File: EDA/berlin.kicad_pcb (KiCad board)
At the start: 2 copper layers, 133 parts, among them SW1 MXSwitch, SW10 MXSwitch, SW100 MXSwitch, SW101 MXSwitch, SW102 MXSwitch, SW103 MXSwitch, SW104 MXSwitch, SW105-1 MXSwitch, SW105-2 MXSwitch, SW106 MXSwitch, SW107 MXSwitch, SW108 MXSwitch, SW109 MXSwitch, SW11 MXSwitch, SW110 MXSwitch, SW111 MXSwitch, SW112 MXSwitch, SW113 MXSwitch, SW114 MXSwitch, SW115 MXSwitch, SW116 MXSwitch, SW117 MXSwitch, SW118 MXSwitch, SW119 MXSwitch, SW12 MXSwitch, SW120 MXSwitch, SW121 MXSwitch, SW122 MXSwitch, SW123 MXSwitch, SW124-1 MXSwitch, SW124-2 MXSwitch, SW125 MXSwitch, SW126 Rotary_Encoder_Switch_Chassis, SW129 MXSwitch, SW13 MXSwitch, SW14 MXSwitch, SW15 MXSwitch, SW16 MXSwitch, SW17 MXSwitch, SW18 MXSwitch, SW19 MXSwitch, SW2 MXSwitch, SW20-1 MXSwitch, SW21 MXSwitch, SW22 MXSwitch, SW23 MXSwitch, SW24 MXSwitch, SW25 MXSwitch, SW26 MXSwitch, SW27 MXSwitch, SW28 MXSwitch, SW29 MXSwitch, SW3 MXSwitch, SW30 MXSwitch, SW31 MXSwitch, SW32 MXSwitch, SW33 MXSwitch, SW34 MXSwitch, SW35 MXSwitch, SW36 MXSwitch, SW37 MXSwitch, SW38 MXSwitch, SW39-1 MXSwitch, SW39-3 MXSwitch, SW4-2 MXSwitch, SW40 MXSwitch, SW41 MXSwitch, SW42 MXSwitch, SW43 MXSwitch, SW44 MXSwitch, SW45 MXSwitch, SW46 MXSwitch, SW47 MXSwitch, SW48 MXSwitch, SW49 MXSwitch, SW5-1 MXSwitch, SW50 MXSwitch, SW51 MXSwitch, SW52 MXSwitch, SW53 MXSwitch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

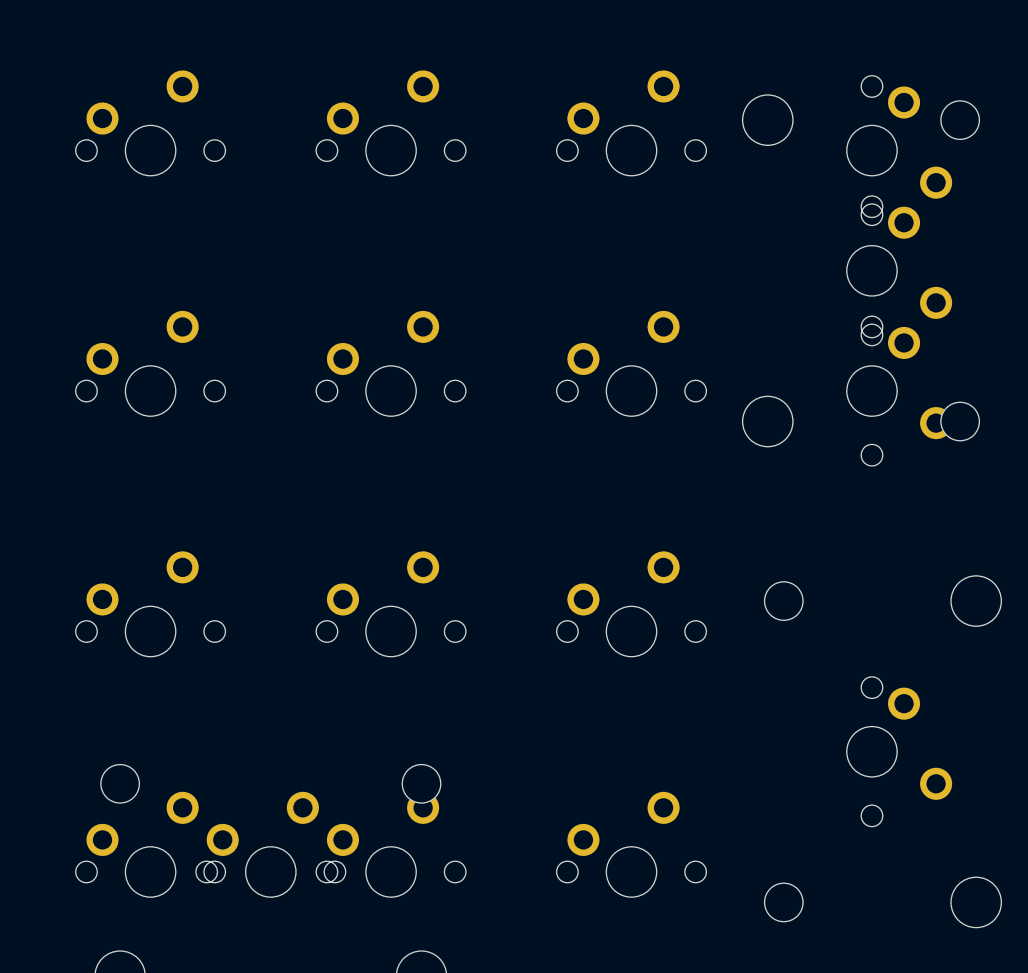
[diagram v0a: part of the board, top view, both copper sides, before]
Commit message: update gitignore and remove unnecessary switches
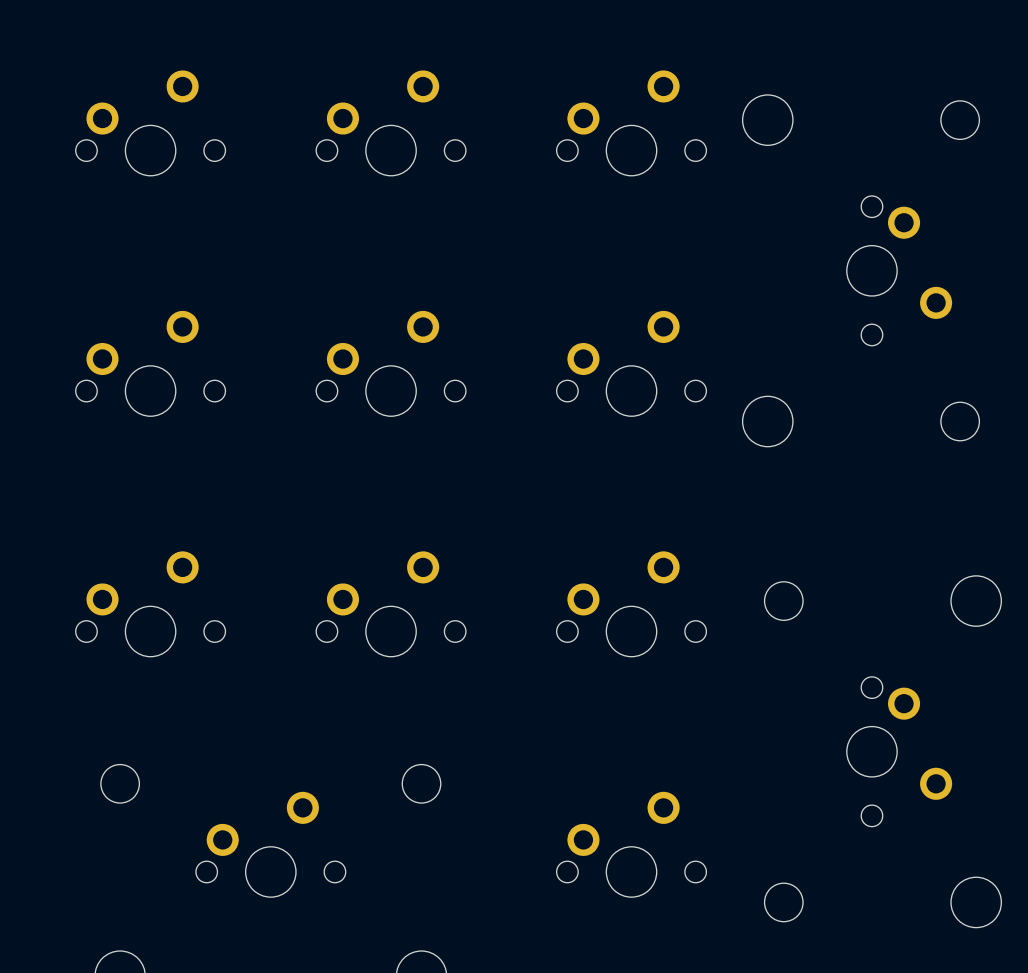
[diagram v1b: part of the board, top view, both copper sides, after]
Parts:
- removed SW105-2, SW112: MXSwitch, acheron_MX:MX100
- removed SW123, SW124-2: MXSwitch, Acheron_MX:MX100

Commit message: bruder muss los
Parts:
- removed the REF** at (441.3, 60.5)
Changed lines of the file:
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@@
     (40 "Dwgs.User" user "User.Drawings")
     (41 "Cmts.User" user "User.Comments")
-    (42 "Eco1.User" user "User.Eco1")
-    (43 "Eco2.User" user "User.Eco2")
     (44 "Edge.Cuts" user)
     (45 "Margin" user)
@@
   )
   (setup
+    (stackup
+      (layer "F.SilkS" (type "Top Silk Screen"))
+      (layer "F.Paste" (type "Top Solder Paste"))
+      (layer "F.Mask" (type "Top Solder Mask") (color "Green") (thickness 0.01))
+      (layer "F.Cu" (type "copper") (thickness 0.035))
+      (layer "dielectric 1" (type "core") (thickness 1.51) (material "FR4") (epsilon_r 4.5) (loss_tangent 0.02))
+      (layer "B.Cu" (type "copper") (thickness 0.035))
+      (layer "B.Mask" (type "Bottom Solder Mask") (color "Green") (thickness 0.01))
+      (layer "B.Paste" (type "Bottom Solder Paste"))
+      (layer "B.SilkS" (type "Bottom Silk Screen"))
+      (copper_finish "None")
+      (dielectric_constraints no)
+    )
     (pad_to_mask_clearance 0)
     (pcbplotparams
@@
     (property "Sheetname" "")
     (attr through_hole)
-    (fp_text reference "SW126" (at 0 0 90) (layer "F.SilkS")
-      (effects (font (size 1 1) (thickness 0.15)))
-    )
-    (fp_text value "Rotary_Encoder_Switch_Chassis" (at 0 -2.5 90) (layer "F.Fab")
+    (fp_text reference "SW126" (at 8.636 -0.12) (layer "F.SilkS")
+      (effects (font (size 1 1) (thickness 0.15)))
+    )
+    (fp_text value "Rotary_Encoder_Switch_Chassis" (at 10.16 0.134) (layer "F.Fab")
       (effects (font (size 1 1) (thickness 0.15)))
     )
@@
     )
   )
-  (footprint "Display:EA_DOGXL160-7_Backlight" (layer "F.Cu")
-    (at 441.325 60.475 -90)
-    (descr "Grapchical,Display,LCD,160x104 http://www.lcd-module.com/eng/pdf/grafik/dogxl160-7e.pdf")
-    (tags "EA_DOGXL160-7_Backlight")
-    (attr through_hole)
-    (fp_text reference "REF**" (at 0.18 -21.02 90) (layer "F.SilkS")
-      (effects (font (size 1 1) (thickness 0.15)))
-    )
-    (fp_text value "EA_DOGXL160-7_Backlight" (at 7.91 59.51 90) (layer "F.Fab")
-      (effects (font (size 1 1) (thickness 0.15)))
-    )
-    (fp_text user "${REFERENCE}" (at 30.48 20.32 90) (layer "F.Fab")
-      (effects (font (size 1 1) (thickness 0.1)))
-    )
-    (fp_line (start -1.82 -20.09) (end -1.82 58.19) (layer "F.SilkS") (width 0.12))
-    (fp_line (start 0.2 -1.35) (end -1.35 -1.35) (layer "F.SilkS") (width 0.12))
-    (fp_line (start -1.82 58.19) (end 62.48 58.19) (layer "F.SilkS") (width 0.12))
-    (fp_line (start 3.1 57.6) (end 55 57.6) (layer "F.SilkS") (width 0.12))
-    (fp_line (start 62.48 -20.09) (end -1.82 -20.09) (layer "F.SilkS") (width 0.12))
-    (fp_line (start -1.35 -1.35) (end -1.35 1) (layer "F.SilkS") (width 0.12))
-    (fp_line (start 62.48 58.19) (end 62.48 -20.09) (layer "F.SilkS") (width 0.12))
-    (fp_line (start 55 57.6) (end 55 -19.5) (layer "F.SilkS") (width 0.12))
-    (fp_line (start 55 -19.5) (end 3.1 -19.5) (layer "F.SilkS") (width 0.12))
-    (fp_line (start 3.1 -19.5) (end 3.1 57.6) (layer "F.SilkS") (width 0.12))
-    (fp_line (start -1.92 -20.2) (end 62.58 -20.2) (layer "F.CrtYd") (width 0.05))
-    (fp_line (start -1.92 58.3) (end -1.92 -20.2) (layer "F.CrtYd") (width 0.05))
-    (fp_line (start 62.58 -20.2) (end 62.58 58.3) (layer "F.CrtYd") (width 0.05))
-    (fp_line (start 62.58 58.3) (end -1.92 58.3) (layer "F.CrtYd") (width 0.05))
-    (fp_line (start 0.34 0) (end -1.66 2) (layer "F.Fab") (width 0.1))
-    (fp_line (start -1.66 -19.95) (end 62.33 -19.95) (layer "F.Fab") (width 0.1))
-    (fp_line (start -1.67 2) (end -1.67 58.05) (layer "F.Fab") (width 0.1))
-    (fp_line (start -1.66 -2) (end -1.66 -19.95) (layer "F.Fab") (width 0.1))
-    (fp_line (start -1.66 -2) (end 0.34 0) (layer "F.Fab") (width 0.1))
-    (fp_line (start 62.33 58.05) (end -1.67 58.05) (layer "F.Fab") (width 0.1))
-    (fp_line (start 62.33 -19.95) (end 62.33 58.05) (layer "F.Fab") (width 0.1))
-    (pad "1" thru_hole rect locked (at 0 0 270) (size 1.524 1.524) (drill 0.762) (layers *.Cu *.Mask))
-    (pad "2" thru_hole circle locked (at 0 2.54 270) (size 1.524 1.524) (drill 0.762) (layers *.Cu *.Mask))
-    (pad "3" thru_hole circle locked (at 0 5.08 270) (size 1.524 1.524) (drill 0.762) (layers *.Cu *.Mask))
-    (pad "14" thru_hole circle locked (at 0 33.02 270) (size 1.524 1.524) (drill 0.762) (layers *.Cu *.Mask))
-    (pad "15" thru_hole circle locked (at 0 35.56 270) (size 1.524 1.524) (drill 0.762) (layers *.Cu *.Mask))
-    (pad "16" thru_hole circle locked (at 0 38.1 270) (size 1.524 1.524) (drill 0.762) (layers *.Cu *.Mask))
-    (pad "17" thru_hole circle locked (at 60.96 38.1 270) (size 1.524 1.524) (drill 0.762) (layers *.Cu *.Mask))
-    (pad "18" thru_hole circle locked (at 60.96 35.56 270) (size 1.524 1.524) (drill 0.762) (layers *.Cu *.Mask))
-    (pad "19" thru_hole circle locked (at 60.96 33.02 270) (size 1.524 1.524) (drill 0.762) (layers *.Cu *.Mask))
-    (pad "20" thru_hole circle locked (at 60.96 30.48 270) (size 1.524 1.524) (drill 0.762) (layers *.Cu *.Mask))
-    (pad "21" thru_hole circle locked (at 60.96 27.94 270) (size 1.524 1.524) (drill 0.762) (layers *.Cu *.Mask))
-    (pad "22" thru_hole circle locked (at 60.96 25.4 270) (size 1.524 1.524) (drill 0.762) (layers *.Cu *.Mask))
-    (pad "23" thru_hole circle locked (at 60.96 22.86 270) (size 1.524 1.524) (drill 0.762) (layers *.Cu *.Mask))
-    (pad "24" thru_hole circle locked (at 60.96 20.32 270) (size 1.524 1.524) (drill 0.762) (layers *.Cu *.Mask))
-    (pad "25" thru_hole circle locked (at 60.96 17.78 270) (size 1.524 1.524) (drill 0.762) (layers *.Cu *.Mask))
-    (pad "26" thru_hole circle locked (at 60.96 15.24 270) (size 1.524 1.524) (drill 0.762) (layers *.Cu *.Mask))
-    (pad "27" thru_hole circle locked (at 60.96 12.7 270) (size 1.524 1.524) (drill 0.762) (layers *.Cu *.Mask))
-    (pad "28" thru_hole circle locked (at 60.96 10.16 270) (size 1.524 1.524) (drill 0.762) (layers *.Cu *.Mask))
-    (pad "29" thru_hole circle locked (at 60.96 7.62 270) (size 1.524 1.524) (drill 0.762) (layers *.Cu *.Mask))
-    (pad "30" thru_hole circle locked (at 60.96 5.08 270) (size 1.524 1.524) (drill 0.762) (layers *.Cu *.Mask))
-    (pad "31" thru_hole circle locked (at 60.96 2.54 270) (size 1.524 1.524) (drill 0.762) (layers *.Cu *.Mask))
-    (pad "32" thru_hole circle locked (at 60.96 0 270) (size 1.524 1.524) (drill 0.762) (layers *.Cu *.Mask))
-    (model "${KICAD6_3DMODEL_DIR}/Display.3dshapes/EA_DOGXL160-7_Backlight.wrl"
-      (offset (xyz 0 0 0))
-      (scale (xyz 1 1 1))
-      (rotate (xyz 0 0 0))
-    )
-  )
   (footprint "acheronHardware:ALPS_EC11E" (layer "F.Cu")
     (at 369.8875 69.85 90)
@@
     (property "Sheetname" "")
     (attr through_hole)
-    (fp_text reference "SW126" (at 0 0 90) (layer "F.SilkS")
-      (effects (font (size 1 1) (thickness 0.15)))
-    )
-    (fp_text value "Rotary_Encoder_Switch_Chassis" (at 0 -2.5 90) (layer "F.Fab")
+    (fp_text reference "SW126" (at 8.89 -0.0635) (layer "F.SilkS")
+      (effects (font (size 1 1) (thickness 0.15)))
+    )
+    (fp_text value "Rotary_Encoder_Switch_Chassis" (at 10.414 -0.0635) (layer "F.Fab")
       (effects (font (size 1 1) (thickness 0.15)))
     )
@@
     (property "Sheetname" "")
     (attr through_hole)
-    (fp_text reference "SW124-1" (at 0 -3.175 90) (layer "Cmts.User")
-      (effects (font (size 1 1) (thickness 0.15) italic))
-    )
-    (fp_text value "MXSwitch" (at 0 -8.7 90) (layer "Cmts.User")
+    (fp_text reference "SW124-1" (at -12.1285 0.03175) (layer "Cmts.User")
+      (effects (font (size 1 1) (thickness 0.15) italic))
+    )
+    (fp_text value "MXSwitch" (at -14.1605 0.03175) (layer "Cmts.User")
       (effects (font (size 1 1) (thickness 0.15)))
     )
@@
     (property "Sheetname" "")
     (attr through_hole)
-    (fp_text reference "SW125" (at 0 -3.175 90) (layer "Cmts.User")
-      (effects (font (size 1 1) (thickness 0.15) italic))
-    )
-    (fp_text value "MXSwitch" (at 0 -6.985 90) (layer "Cmts.User")
-      (effects (font (size 1 1) (thickness 0.15)))
-    )
+    (fp_text reference "SW125" (at -12.1285 0.03175) (layer "Cmts.User")
+      (effects (font (size 1 1) (thickness 0.15) italic))
+    )
+    (fp_text value "MXSwitch" (at -14.1605 0.03175) (layer "Cmts.User")
+      (effects (font (size 1 1) (thickness 0.15)))
+    )

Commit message: update/fix switch descriptors
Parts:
- SW125: value MXSwitch -> 2,19
- renumbered SW126 to SW1,1, SW58 to SW1,10, SW65 to SW1,11, SW72 to SW1,12, SW79 to SW1,13, SW86 to SW1,14, SW93 to SW1,15, SW126 to SW1,16, SW7 to SW1,2, SW14 to SW1,3, SW21 to SW1,4, SW27 to SW1,5, SW33 to SW1,6, SW40 to SW1,7, SW46 to SW1,8, SW52 to SW1,9, SW1 to SW2,1, SW59 to SW2,10, SW66 to SW2,11, SW73 to SW2,12, SW80 to SW2,13, SW86 to SW2,14, SW93 to SW2,15, SW99 to SW2,16, SW122 to SW2,17, SW124-1 to SW2,18, SW8 to SW2,2, SW15 to SW2,3, SW22 to SW2,4, SW28 to SW2,5, SW34 to SW2,6, SW41 to SW2,7, SW47 to SW2,8, SW53 to SW2,9, SW2 to SW3,1, SW60 to SW3,10, SW67 to SW3,11, SW74 to SW3,12, SW81 to SW3,13, SW87 to SW3,14, SW94 to SW3,15, SW100 to SW3,16, SW101 to SW3,17, SW108 to SW3,18, SW115 to SW3,19, SW9 to SW3,2, SW16 to SW3,3, SW23 to SW3,4, SW29 to SW3,5, SW35 to SW3,6, SW42 to SW3,7, SW48 to SW3,8, SW54 to SW3,9, SW3 to SW4,1, SW61 to SW4,10, SW68 to SW4,11, SW75 to SW4,12, SW88-2 to SW4,13, SW106 to SW4,14, SW113 to SW4,15, SW120 to SW4,16, SW102 to SW4,17, SW109 to SW4,18, SW116 to SW4,19, SW10 to SW4,2, SW17 to SW4,3, SW24 to SW4,4, SW30 to SW4,5, SW36 to SW4,6, SW43 to SW4,7, SW49 to SW4,8, SW55 to SW4,9, SW4-2 to SW5,1, SW62 to SW5,10, SW69 to SW5,11, SW76 to SW5,12, SW82 to SW5,13, SW107 to SW5,14, SW114 to SW5,15, SW121 to SW5,16, SW103 to SW5,17, SW110 to SW5,18, SW117 to SW5,19, SW11 to SW5,2, SW18 to SW5,3, SW25 to SW5,4, SW31 to SW5,5, SW37 to SW5,6, SW44 to SW5,7, SW50 to SW5,8, SW56 to SW5,9, SW5-1 to SW6,1, SW63 to SW6,10, SW70 to SW6,11, SW83 to SW6,12, SW90-2 to SW6,13, SW91 to SW6,15, SW104 to SW6,17, SW111 to SW6,18, SW118 to SW6,19, SW12 to SW6,2, SW19 to SW6,3, SW26 to SW6,4, SW32 to SW6,5, SW38 to SW6,6, SW45 to SW6,7, SW51 to SW6,8, SW57 to SW6,9, SW6-1 to SW7,1, SW20-1 to SW7,10, SW20-1 to SW7,11, SW77 to SW7,12, SW129 to SW7,13, SW85 to SW7,14, SW92 to SW7,15, SW98 to SW7,16, SW105-1 to SW7,17, SW119 to SW7,19, SW13 to SW7,2, SW39-3 to SW7,3, SW39-1 to SW7,6, SW20-1 to SW7,8, SW20-1 to SW7,9

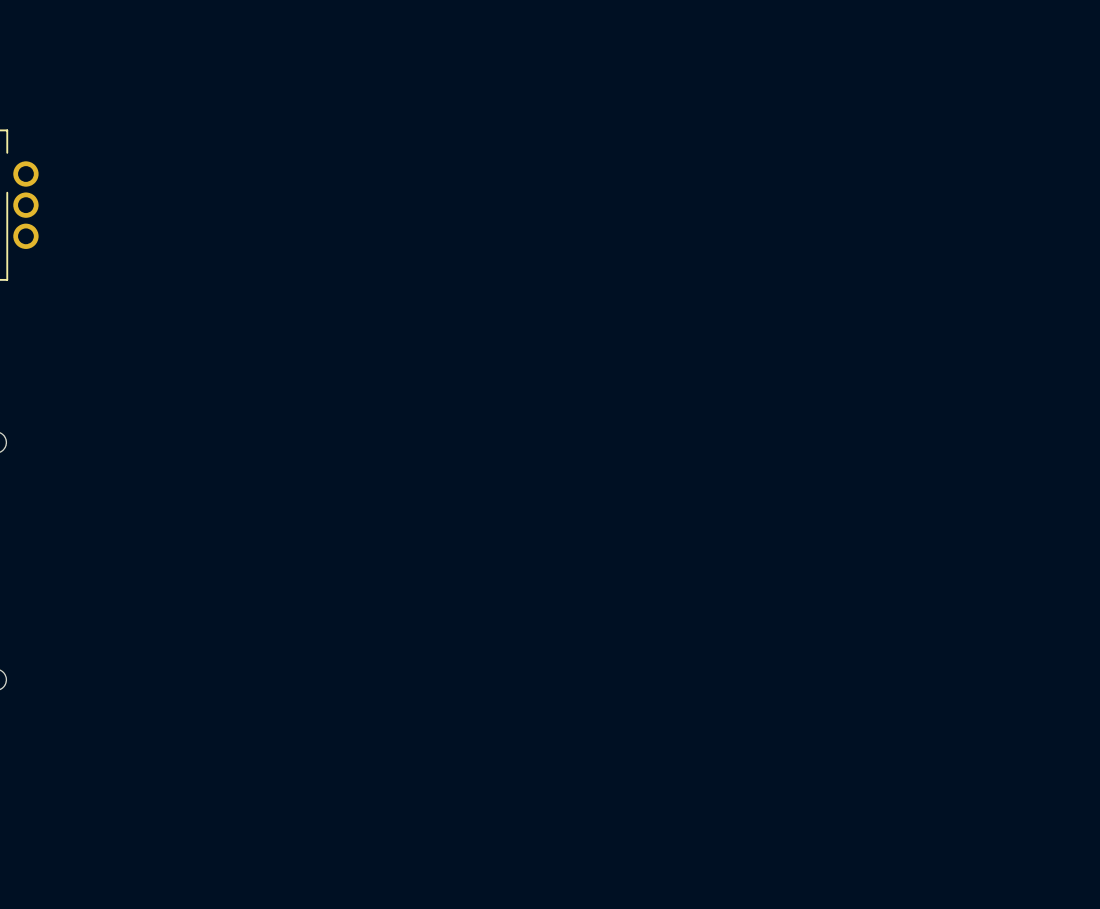
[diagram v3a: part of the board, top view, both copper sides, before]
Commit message: Add DOGXL LCD to PCB
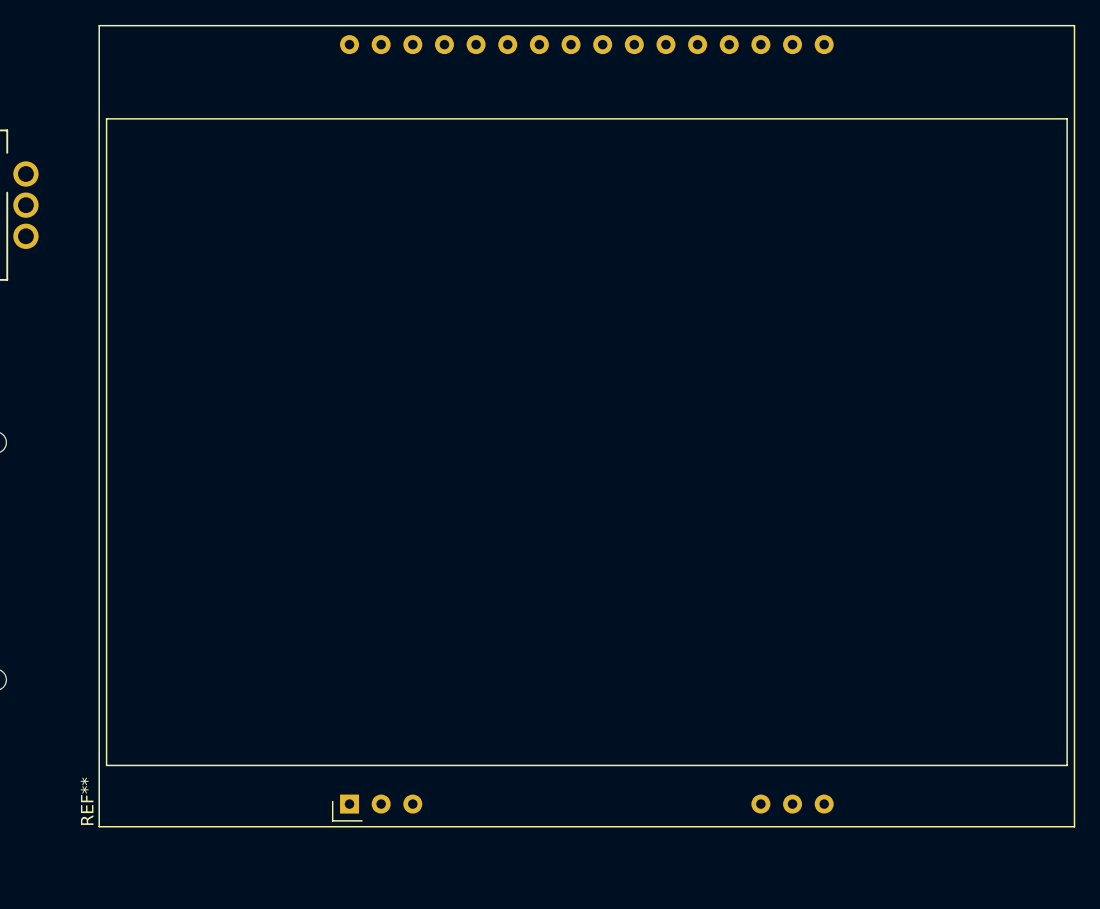
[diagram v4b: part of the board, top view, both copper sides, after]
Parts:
- added REF**: EA_DOGXL160-7_Backlight, Display:EA_DOGXL160-7_Backlight, F.Cu at (403.4, 117.9)
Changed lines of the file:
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@@
+    )
+  )
+  (footprint "Display:EA_DOGXL160-7_Backlight" (layer "F.Cu")
+    (at 403.359915 117.923454 90)
+    (descr "Grapchical,Display,LCD,160x104 http://www.lcd-module.com/eng/pdf/grafik/dogxl160-7e.pdf")
+    (tags "EA_DOGXL160-7_Backlight")
+    (attr through_hole)
+    (fp_text reference "REF**" (at 0.18 -21.02 90) (layer "F.SilkS")
+      (effects (font (size 1 1) (thickness 0.15)))
+    )
+    (fp_text value "EA_DOGXL160-7_Backlight" (at 7.91 59.51 90) (layer "F.Fab")
+      (effects (font (size 1 1) (thickness 0.15)))
+    )
+    (fp_text user "${REFERENCE}" (at 30.48 20.32 90) (layer "F.Fab")
+      (effects (font (size 1 1) (thickness 0.1)))
+    )
+    (fp_line (start -1.82 58.19) (end 62.48 58.19) (layer "F.SilkS") (width 0.12))
+    (fp_line (start 62.48 58.19) (end 62.48 -20.09) (layer "F.SilkS") (width 0.12))
+    (fp_line (start 55 -19.5) (end 3.1 -19.5) (layer "F.SilkS") (width 0.12))
+    (fp_line (start 0.2 -1.35) (end -1.35 -1.35) (layer "F.SilkS") (width 0.12))
+    (fp_line (start -1.35 -1.35) (end -1.35 1) (layer "F.SilkS") (width 0.12))
+    (fp_line (start 62.48 -20.09) (end -1.82 -20.09) (layer "F.SilkS") (width 0.12))
+    (fp_line (start 55 57.6) (end 55 -19.5) (layer "F.SilkS") (width 0.12))
+    (fp_line (start -1.82 -20.09) (end -1.82 58.19) (layer "F.SilkS") (width 0.12))
+    (fp_line (start 3.1 -19.5) (end 3.1 57.6) (layer "F.SilkS") (width 0.12))
+    (fp_line (start 3.1 57.6) (end 55 57.6) (layer "F.SilkS") (width 0.12))
+    (fp_line (start 62.58 58.3) (end -1.92 58.3) (layer "F.CrtYd") (width 0.05))
+    (fp_line (start -1.92 58.3) (end -1.92 -20.2) (layer "F.CrtYd") (width 0.05))
+    (fp_line (start 62.58 -20.2) (end 62.58 58.3) (layer "F.CrtYd") (width 0.05))
+    (fp_line (start -1.92 -20.2) (end 62.58 -20.2) (layer "F.CrtYd") (width 0.05))
+    (fp_line (start -1.66 -19.95) (end 62.33 -19.95) (layer "F.Fab") (width 0.1))
+    (fp_line (start 62.33 -19.95) (end 62.33 58.05) (layer "F.Fab") (width 0.1))
+    (fp_line (start 0.34 0) (end -1.66 2) (layer "F.Fab") (width 0.1))
+    (fp_line (start 62.33 58.05) (end -1.67 58.05) (layer "F.Fab") (width 0.1))
+    (fp_line (start -1.67 2) (end -1.67 58.05) (layer "F.Fab") (width 0.1))
+    (fp_line (start -1.66 -2) (end 0.34 0) (layer "F.Fab") (width 0.1))
+    (fp_line (start -1.66 -2) (end -1.66 -19.95) (layer "F.Fab") (width 0.1))
+    (pad "1" thru_hole rect locked (at 0 0 90) (size 1.524 1.524) (drill 0.762) (layers *.Cu *.Mask))
+    (pad "2" thru_hole circle locked (at 0 2.54 90) (size 1.524 1.524) (drill 0.762) (layers *.Cu *.Mask))
+    (pad "3" thru_hole circle locked (at 0 5.08 90) (size 1.524 1.524) (drill 0.762) (layers *.Cu *.Mask))
+    (pad "14" thru_hole circle locked (at 0 33.02 90) (size 1.524 1.524) (drill 0.762) (layers *.Cu *.Mask))
+    (pad "15" thru_hole circle locked (at 0 35.56 90) (size 1.524 1.524) (drill 0.762) (layers *.Cu *.Mask))
+    (pad "16" thru_hole circle locked (at 0 38.1 90) (size 1.524 1.524) (drill 0.762) (layers *.Cu *.Mask))
+    (pad "17" thru_hole circle locked (at 60.96 38.1 90) (size 1.524 1.524) (drill 0.762) (layers *.Cu *.Mask))
+    (pad "18" thru_hole circle locked (at 60.96 35.56 90) (size 1.524 1.524) (drill 0.762) (layers *.Cu *.Mask))
+    (pad "19" thru_hole circle locked (at 60.96 33.02 90) (size 1.524 1.524) (drill 0.762) (layers *.Cu *.Mask))
+    (pad "20" thru_hole circle locked (at 60.96 30.48 90) (size 1.524 1.524) (drill 0.762) (layers *.Cu *.Mask))
+    (pad "21" thru_hole circle locked (at 60.96 27.94 90) (size 1.524 1.524) (drill 0.762) (layers *.Cu *.Mask))
+    (pad "22" thru_hole circle locked (at 60.96 25.4 90) (size 1.524 1.524) (drill 0.762) (layers *.Cu *.Mask))
+    (pad "23" thru_hole circle locked (at 60.96 22.86 90) (size 1.524 1.524) (drill 0.762) (layers *.Cu *.Mask))
+    (pad "24" thru_hole circle locked (at 60.96 20.32 90) (size 1.524 1.524) (drill 0.762) (layers *.Cu *.Mask))
+    (pad "25" thru_hole circle locked (at 60.96 17.78 90) (size 1.524 1.524) (drill 0.762) (layers *.Cu *.Mask))
+    (pad "26" thru_hole circle locked (at 60.96 15.24 90) (size 1.524 1.524) (drill 0.762) (layers *.Cu *.Mask))
+    (pad "27" thru_hole circle locked (at 60.96 12.7 90) (size 1.524 1.524) (drill 0.762) (layers *.Cu *.Mask))
+    (pad "28" thru_hole circle locked (at 60.96 10.16 90) (size 1.524 1.524) (drill 0.762) (layers *.Cu *.Mask))
+    (pad "29" thru_hole circle locked (at 60.96 7.62 90) (size 1.524 1.524) (drill 0.762) (layers *.Cu *.Mask))
+    (pad "30" thru_hole circle locked (at 60.96 5.08 90) (size 1.524 1.524) (drill 0.762) (layers *.Cu *.Mask))
+    (pad "31" thru_hole circle locked (at 60.96 2.54 90) (size 1.524 1.524) (drill 0.762) (layers *.Cu *.Mask))
+    (pad "32" thru_hole circle locked (at 60.96 0 90) (size 1.524 1.524) (drill 0.762) (layers *.Cu *.Mask))
+    (model "${KICAD6_3DMODEL_DIR}/Display.3dshapes/EA_DOGXL160-7_Backlight.wrl"
+      (offset (xyz 0 0 0))
+      (scale (xyz 1 1 1))
+      (rotate (xyz 0 0 0))
     )
   )
